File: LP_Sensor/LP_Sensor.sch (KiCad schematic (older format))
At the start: 0 parts

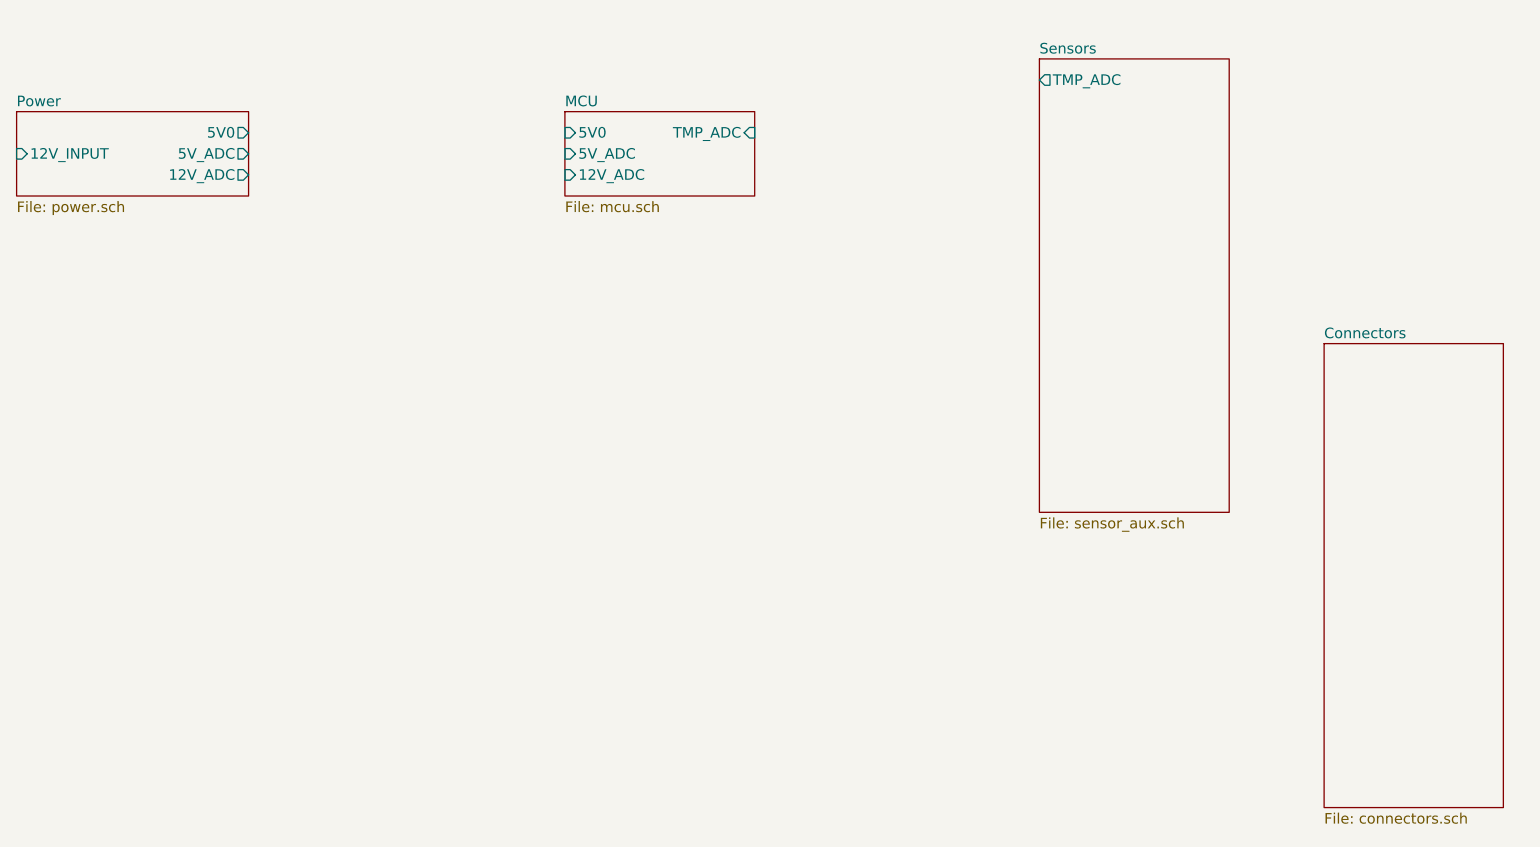
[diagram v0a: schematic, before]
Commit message: Added IMU to Sensor page.
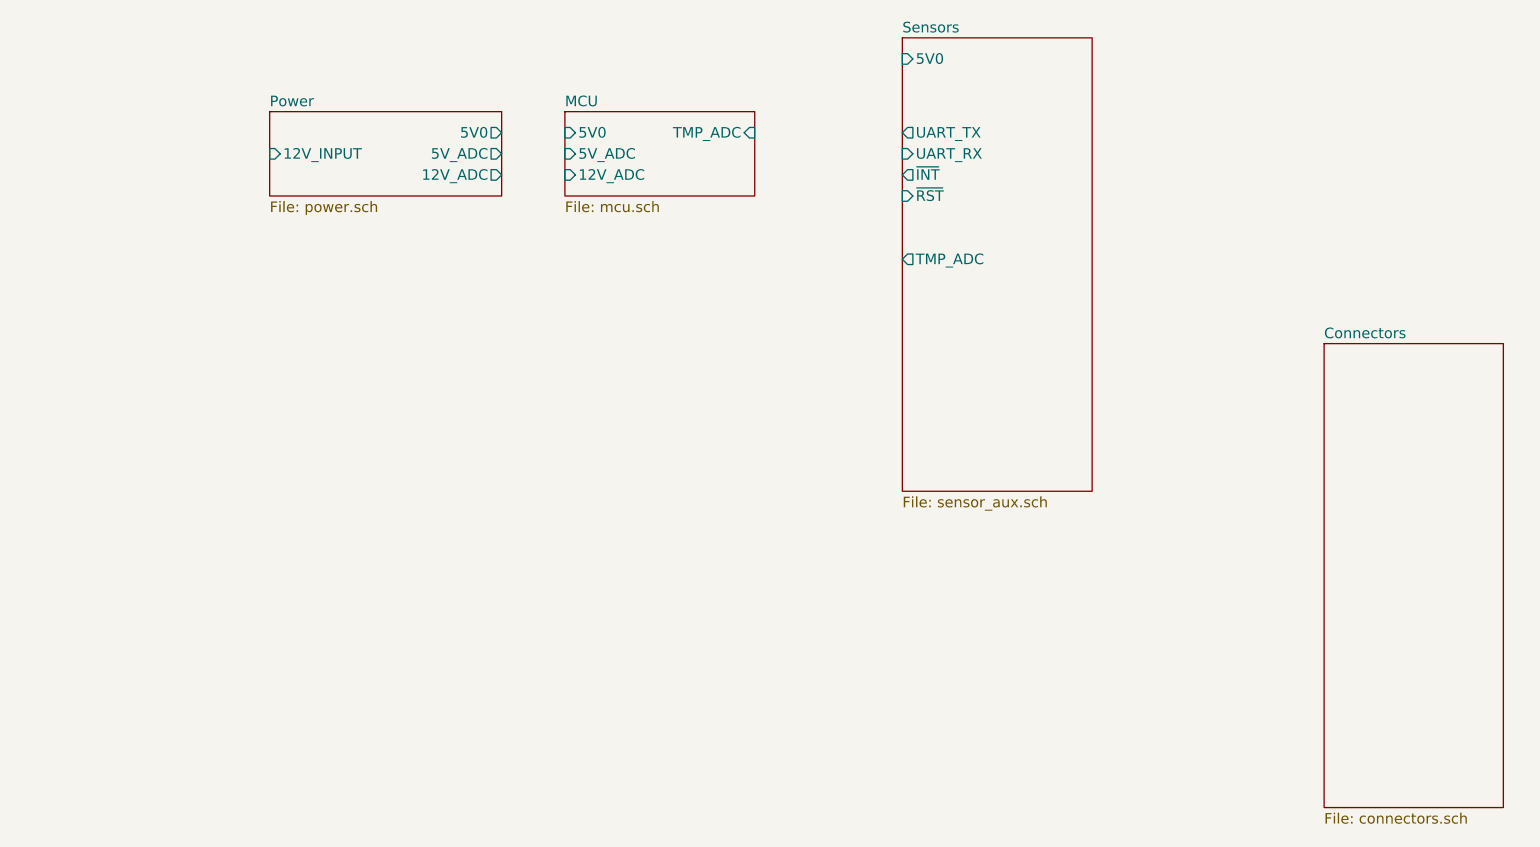
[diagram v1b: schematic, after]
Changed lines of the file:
@@
 $EndDescr
 $Sheet
-S 1500 1000 1100 400
+S 2700 1000 1100 400
 U 6122AB04
 F0 "Power" 50
 F1 "power.sch" 50
-F2 "5V0" O R 2600 1100 50
-F3 "12V_INPUT" I L 1500 1200 50
-F4 "5V_ADC" O R 2600 1200 50
-F5 "12V_ADC" O R 2600 1300 50
+F2 "5V0" O R 3800 1100 50
+F3 "12V_INPUT" I L 2700 1200 50
+F4 "5V_ADC" O R 3800 1200 50
+F5 "12V_ADC" O R 3800 1300 50
 $EndSheet
 $Sheet
@@
 $EndSheet
 $Sheet
-S 6350 750  900  2150
+S 5700 650  900  2150
 U 6122ACAD
 F0 "Sensors" 50
 F1 "sensor_aux.sch" 50
-F2 "TMP_ADC" O L 6350 850 50
+F2 "TMP_ADC" O L 5700 1700 50
+F3 "5V0" I L 5700 750 50
+F4 "UART_TX" O L 5700 1100 50
+F5 "UART_RX" I L 5700 1200 50
+F6 "~INT" O L 5700 1300 50
+F7 "~RST" I L 5700 1400 50
 $EndSheet
 $EndSCHEMATC
